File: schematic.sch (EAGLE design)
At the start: 8 parts, among them T1 BC547, X1 HD44780LCD-1602

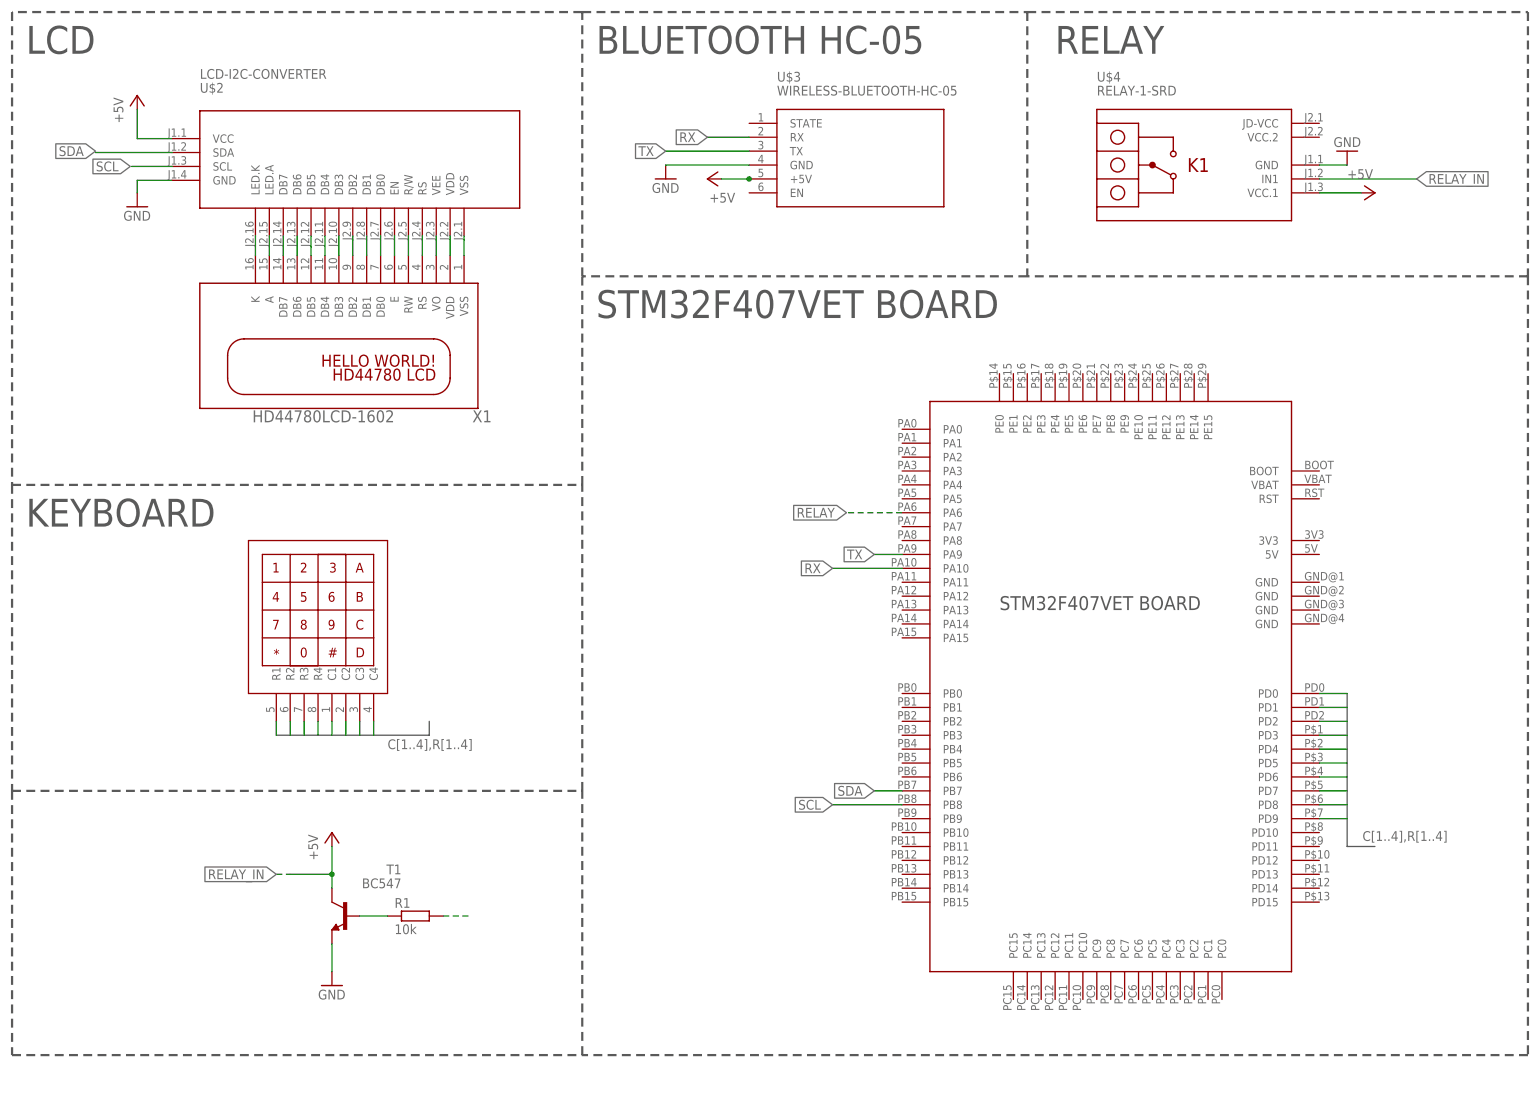
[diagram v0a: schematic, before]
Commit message: add leds
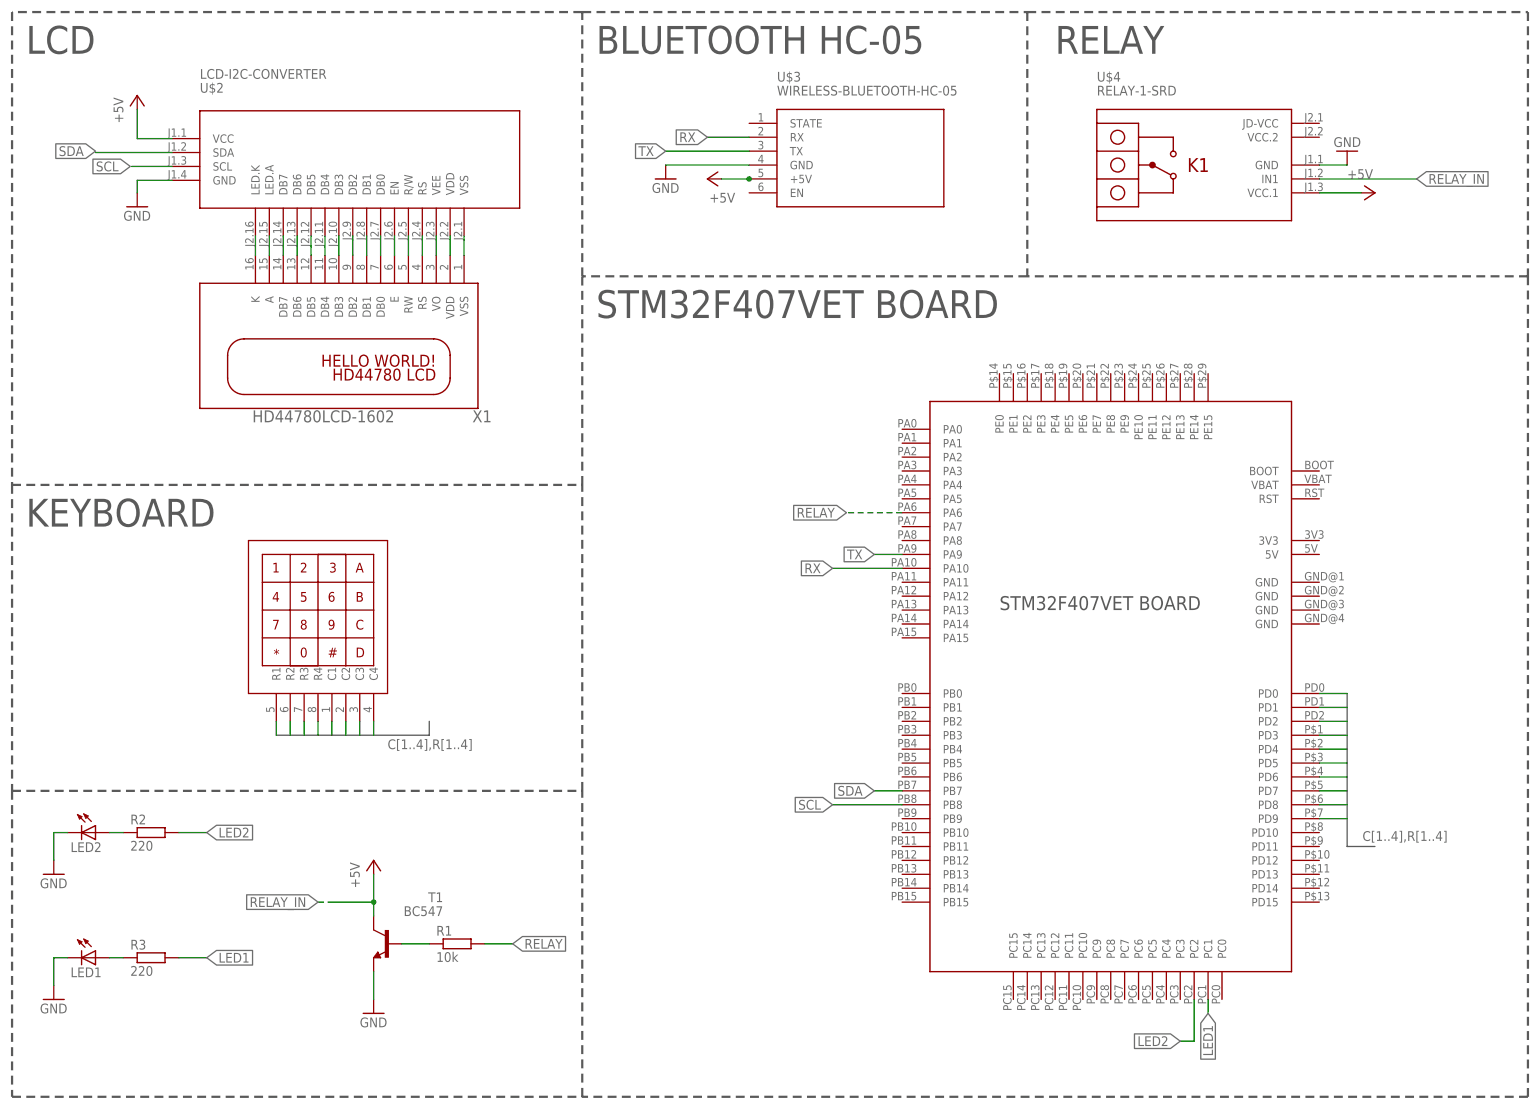
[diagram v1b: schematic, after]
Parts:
- added LED1, LED2: (no value), adafruit:LED
- added R2, R3: 220, resistor:R-EU_R1206
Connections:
- removed net N$16: R1.2
- new net LED1: R3.2, U$5.PC1
- new net LED2: R2.2, U$5.PC2
- new net N$17: LED2.A, R2.1
- new net N$18: LED1.A, R3.1
- net GND: now also LED1.C, LED2.C
- net RELAY: now also R1.2
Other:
- moved on the sheet: R1, T1
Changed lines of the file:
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@@
 <part name="GND4" library="supply1" library_urn="urn:adsk.eagle:library:371" deviceset="GND" device=""/>
 <part name="U$5" library="stm32_discovery" deviceset="STM32_DISCOVERY" device=""/>
+<part name="LED1" library="adafruit" library_urn="urn:adsk.eagle:library:420" deviceset="LED" device="" package3d_urn="urn:adsk.eagle:package:6240563/1"/>
+<part name="LED2" library="adafruit" library_urn="urn:adsk.eagle:library:420" deviceset="LED" device="" package3d_urn="urn:adsk.eagle:package:6240563/1"/>
+<part name="R2" library="resistor" library_urn="urn:adsk.eagle:library:348" deviceset="R-EU_" device="R1206" package3d_urn="urn:adsk.eagle:package:26062/1" value="220"/>
+<part name="R3" library="resistor" library_urn="urn:adsk.eagle:library:348" deviceset="R-EU_" device="R1206" package3d_urn="urn:adsk.eagle:package:26062/1" value="220"/>
+<part name="GND5" library="supply1" library_urn="urn:adsk.eagle:library:371" deviceset="GND" device=""/>
+<part name="GND6" library="supply1" library_urn="urn:adsk.eagle:library:371" deviceset="GND" device=""/>
 </parts>
 <sheets>
@@
 <wire x1="-88.9" y1="48.26" x2="15.24" y2="48.26" width="0.4064" layer="97" style="longdash"/>
 <wire x1="15.24" y1="48.26" x2="15.24" y2="104.14" width="0.4064" layer="97" style="longdash"/>
-<wire x1="-88.9" y1="48.26" x2="-88.9" y2="0" width="0.4064" layer="97" style="longdash"/>
-<wire x1="-88.9" y1="0" x2="15.24" y2="0" width="0.4064" layer="97" style="longdash"/>
-<wire x1="15.24" y1="0" x2="15.24" y2="48.26" width="0.4064" layer="97" style="longdash"/>
-<wire x1="187.96" y1="142.24" x2="187.96" y2="0" width="0.4064" layer="97" style="longdash"/>
-<wire x1="187.96" y1="0" x2="15.24" y2="0" width="0.4064" layer="97" style="longdash"/>
+<wire x1="-88.9" y1="48.26" x2="-88.9" y2="-7.62" width="0.4064" layer="97" style="longdash"/>
+<wire x1="-88.9" y1="-7.62" x2="15.24" y2="-7.62" width="0.4064" layer="97" style="longdash"/>
+<wire x1="15.24" y1="-7.62" x2="15.24" y2="48.26" width="0.4064" layer="97" style="longdash"/>
+<wire x1="187.96" y1="142.24" x2="187.96" y2="-7.62" width="0.4064" layer="97" style="longdash"/>
+<wire x1="187.96" y1="-7.62" x2="15.24" y2="-7.62" width="0.4064" layer="97" style="longdash"/>
 <text x="-86.36" y="182.88" size="5.08" layer="97">LCD</text>
 <text x="17.78" y="182.88" size="5.08" layer="97">BLUETOOTH HC-05</text>
@@
 <attribute name="VALUE" x="109.22" y="175.26" size="1.778" layer="95"/>
 </instance>
-<instance part="T1" gate="G$1" x="-27.94" y="25.4" smashed="yes" rot="MR0">
-<attribute name="NAME" x="-17.78" y="33.02" size="1.778" layer="95" rot="MR0"/>
-<attribute name="VALUE" x="-17.78" y="30.48" size="1.778" layer="96" rot="MR0"/>
-</instance>
-<instance part="R1" gate="G$1" x="-15.24" y="25.4" smashed="yes">
-<attribute name="NAME" x="-19.05" y="26.8986" size="1.778" layer="95"/>
-<attribute name="VALUE" x="-19.05" y="22.098" size="1.778" layer="96"/>
-</instance>
-<instance part="GND1" gate="1" x="-30.48" y="12.7" smashed="yes">
-<attribute name="VALUE" x="-33.02" y="10.16" size="1.778" layer="96"/>
-</instance>
-<instance part="P+1" gate="1" x="-30.48" y="40.64" smashed="yes">
-<attribute name="VALUE" x="-33.02" y="35.56" size="1.778" layer="96" rot="R90"/>
+<instance part="T1" gate="G$1" x="-20.32" y="20.32" smashed="yes" rot="MR0">
+<attribute name="NAME" x="-10.16" y="27.94" size="1.778" layer="95" rot="MR0"/>
+<attribute name="VALUE" x="-10.16" y="25.4" size="1.778" layer="96" rot="MR0"/>
+</instance>
+<instance part="R1" gate="G$1" x="-7.62" y="20.32" smashed="yes">
+<attribute name="NAME" x="-11.43" y="21.8186" size="1.778" layer="95"/>
+<attribute name="VALUE" x="-11.43" y="17.018" size="1.778" layer="96"/>
+</instance>
+<instance part="GND1" gate="1" x="-22.86" y="7.62" smashed="yes">
+<attribute name="VALUE" x="-25.4" y="5.08" size="1.778" layer="96"/>
+</instance>
+<instance part="P+1" gate="1" x="-22.86" y="35.56" smashed="yes">
+<attribute name="VALUE" x="-25.4" y="30.48" size="1.778" layer="96" rot="R90"/>
 </instance>
 <instance part="P+2" gate="1" x="160.02" y="157.48" smashed="yes" rot="R270">
@@
 </instance>
 <instance part="U$5" gate="G$1" x="121.92" y="66.04" smashed="yes"/>
+<instance part="LED1" gate="G$1" x="-73.66" y="17.78" smashed="yes" rot="R270">
+<attribute name="NAME" x="-78.232" y="14.224" size="1.778" layer="95"/>
+<attribute name="VALUE" x="-78.232" y="12.065" size="1.778" layer="96"/>
+</instance>
+<instance part="LED2" gate="G$1" x="-73.66" y="40.64" smashed="yes" rot="R270">
+<attribute name="NAME" x="-78.232" y="37.084" size="1.778" layer="95"/>
+<attribute name="VALUE" x="-78.232" y="34.925" size="1.778" layer="96"/>
+</instance>
+<instance part="R2" gate="G$1" x="-63.5" y="40.64" smashed="yes">
+<attribute name="NAME" x="-67.31" y="42.1386" size="1.778" layer="95"/>
+<attribute name="VALUE" x="-67.31" y="37.338" size="1.778" layer="96"/>
+</instance>
+<instance part="R3" gate="G$1" x="-63.5" y="17.78" smashed="yes">
+<attribute name="NAME" x="-67.31" y="19.2786" size="1.778" layer="95"/>
+<attribute name="VALUE" x="-67.31" y="14.478" size="1.778" layer="96"/>
+</instance>
+<instance part="GND5" gate="1" x="-81.28" y="33.02" smashed="yes">
+<attribute name="VALUE" x="-83.82" y="30.48" size="1.778" layer="96"/>
+</instance>
+<instance part="GND6" gate="1" x="-81.28" y="10.16" smashed="yes">
+<attribute name="VALUE" x="-83.82" y="7.62" size="1.778" layer="96"/>
+</instance>
 </instances>
 <busses>
@@
 <pinref part="T1" gate="G$1" pin="B"/>
 <pinref part="R1" gate="G$1" pin="1"/>
-<wire x1="-25.4" y1="25.4" x2="-20.32" y2="25.4" width="0.1524" layer="91"/>
+<wire x1="-17.78" y1="20.32" x2="-12.7" y2="20.32" width="0.1524" layer="91"/>
 </segment>
 </net>
@@
 <pinref part="T1" gate="G$1" pin="E"/>
 <pinref part="GND1" gate="1" pin="GND"/>
-<wire x1="-30.48" y1="20.32" x2="-30.48" y2="15.24" width="0.1524" layer="91"/>
+<wire x1="-22.86" y1="15.24" x2="-22.86" y2="10.16" width="0.1524" layer="91"/>
 </segment>
 <segment>
@@
 <wire x1="45.72" y1="162.56" x2="30.48" y2="162.56" width="0.1524" layer="91"/>
 </segment>
+<segment>
+<pinref part="LED2" gate="G$1" pin="C"/>
+<pinref part="GND5" gate="1" pin="GND"/>
+<wire x1="-78.74" y1="40.64" x2="-81.28" y2="40.64" width="0.1524" layer="91"/>
+<wire x1="-81.28" y1="40.64" x2="-81.28" y2="35.56" width="0.1524" layer="91"/>
+</segment>
+<segment>
+<pinref part="LED1" gate="G$1" pin="C"/>
+<pinref part="GND6" gate="1" pin="GND"/>
+<wire x1="-78.74" y1="17.78" x2="-81.28" y2="17.78" width="0.1524" layer="91"/>
+<wire x1="-81.28" y1="17.78" x2="-81.28" y2="12.7" width="0.1524" layer="91"/>
+</segment>
 </net>
 <net name="RELAY_IN" class="0">
@@
 <pinref part="P+1" gate="1" pin="+5V"/>
 <pinref part="T1" gate="G$1" pin="C"/>
-<wire x1="-30.48" y1="38.1" x2="-30.48" y2="33.02" width="0.1524" layer="91"/>
-<wire x1="-30.48" y1="33.02" x2="-30.48" y2="30.48" width="0.1524" layer="91"/>
-<wire x1="-30.48" y1="33.02" x2="-38.1" y2="33.02" width="0.1524" layer="91"/>
-<junction x="-30.48" y="33.02"/>
-<label x="-40.64" y="33.02" size="1.778" layer="95" rot="R180" xref="yes"/>
-<wire x1="-40.64" y1="33.02" x2="-38.1" y2="33.02" width="0.1524" layer="91" style="longdash"/>
+<wire x1="-22.86" y1="33.02" x2="-22.86" y2="27.94" width="0.1524" layer="91"/>
+<wire x1="-22.86" y1="27.94" x2="-22.86" y2="25.4" width="0.1524" layer="91"/>
+<wire x1="-22.86" y1="27.94" x2="-30.48" y2="27.94" width="0.1524" layer="91"/>
+<junction x="-22.86" y="27.94"/>
+<label x="-33.02" y="27.94" size="1.778" layer="95" rot="R180" xref="yes"/>
+<wire x1="-33.02" y1="27.94" x2="-30.48" y2="27.94" width="0.1524" layer="91" style="longdash"/>
 </segment>
 <segment>
@@
 <label x="63.5" y="99.06" size="1.778" layer="95" rot="R180" xref="yes"/>
 </segment>
-</net>
-<net name="N$16" class="0">
 <segment>
 <pinref part="R1" gate="G$1" pin="2"/>
-<wire x1="-10.16" y1="25.4" x2="-5.08" y2="25.4" width="0.1524" layer="91" style="longdash"/>
-</segment>
-</net>
+<wire x1="-2.54" y1="20.32" x2="2.54" y2="20.32" width="0.1524" layer="91"/>
+<label x="2.54" y="20.32" size="1.778" layer="95" xref="yes"/>
+</segment>
+</net>
+<net name="LED1" class="0">
+<segment>
+<pinref part="U$5" gate="G$1" pin="PC1"/>
+<wire x1="129.54" y1="10.16" x2="129.54" y2="7.62" width="0.1524" layer="91"/>
+<label x="129.54" y="7.62" size="1.778" layer="95" rot="R270" xref="yes"/>
+</segment>
+<segment>
+<pinref part="R3" gate="G$1" pin="2"/>
+<wire x1="-58.42" y1="17.78" x2="-53.34" y2="17.78" width="0.1524" layer="91"/>
+<label x="-53.34" y="17.78" size="1.778" layer="95" xref="yes"/>
+</segment>
+</net>
+<net name="LED2" class="0">
+<segment>
+<pinref part="U$5" gate="G$1" pin="PC2"/>
+<wire x1="127" y1="10.16" x2="127" y2="2.54" width="0.1524" layer="91"/>
+<wire x1="127" y1="2.54" x2="124.46" y2="2.54" width="0.1524" layer="91"/>
+<label x="124.46" y="2.54" size="1.778" layer="95" rot="R180" xref="yes"/>
+</segment>
+<segment>
+<pinref part="R2" gate="G$1" pin="2"/>
+<wire x1="-58.42" y1="40.64" x2="-53.34" y2="40.64" width="0.1524" layer="91"/>
+<label x="-53.34" y="40.64" size="1.778" layer="95" xref="yes"/>
+</segment>
+</net>
+<net name="N$17" class="0">
+<segment>
+<pinref part="R2" gate="G$1" pin="1"/>
+<pinref part="LED2" gate="G$1" pin="A"/>
+<wire x1="-68.58" y1="40.64" x2="-71.12" y2="40.64" width="0.1524" layer="91"/>
+</segment>
+</net>
+<net name="N$18" class="0">
+<segment>
+<pinref part="R3" gate="G$1" pin="1"/>
+<pinref part="LED1" gate="G$1" pin="A"/>
+<wire x1="-68.58" y1="17.78" x2="-71.12" y2="17.78" width="0.1524" layer="91"/>
+</segment>
+</net>
